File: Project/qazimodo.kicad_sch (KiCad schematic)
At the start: 24 parts, among them J1 AVR-ISP-6, J2 Conn_01x04_MountingPin, J3 USB_C_Receptacle_USB2.0, U1 ATmega32U4-M, Y1 Crystal_GND24_Small

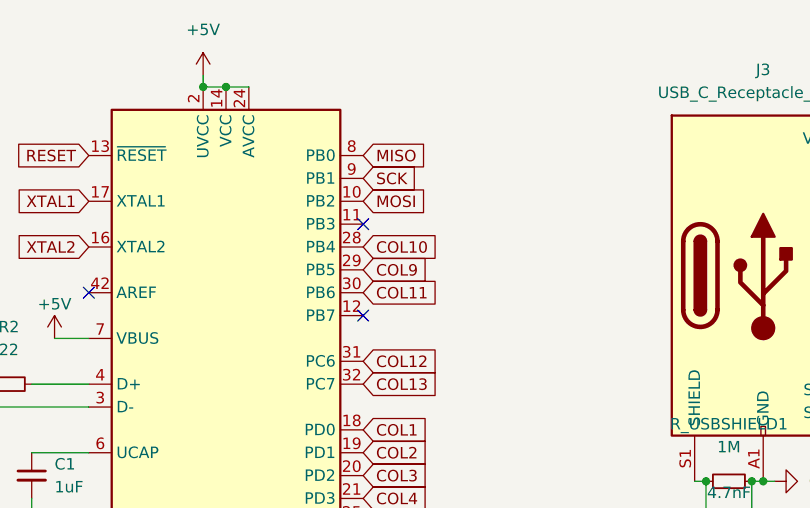
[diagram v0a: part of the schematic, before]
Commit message: matrix issues deteced and fixed, needs new silkscreen
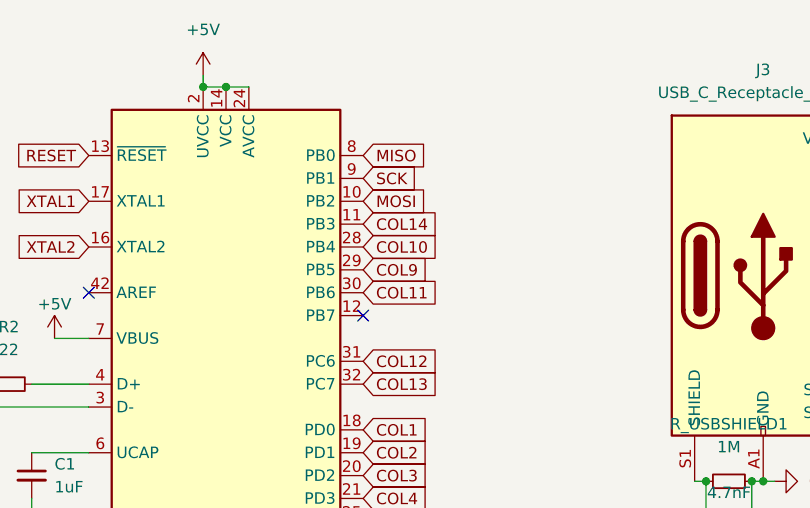
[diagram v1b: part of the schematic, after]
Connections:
- net COL14: now reaches U1.11 (PB3)
- no-connect marks 4 -> 3
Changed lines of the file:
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@@
   )
   (no_connect (at 39.37 45.085))
-  (no_connect (at 69.85 37.465))
   (no_connect (at 69.85 47.625))
   (no_connect (at 69.85 85.725))
@@
       (effects (font (size 1.27 1.27)) (justify left) hide)
     )
+  )
+  (global_label "COL14" (shape input) (at 69.85 37.465 0) (fields_autoplaced)
+    (effects (font (size 1.27 1.27)) (justify left))
+    (property "Intersheetrefs" "${INTERSHEET_REFS}" (at 78.8034 37.465 0)
+      (effects (font (size 1.27 1.27)) (justify left) hide)
+    )

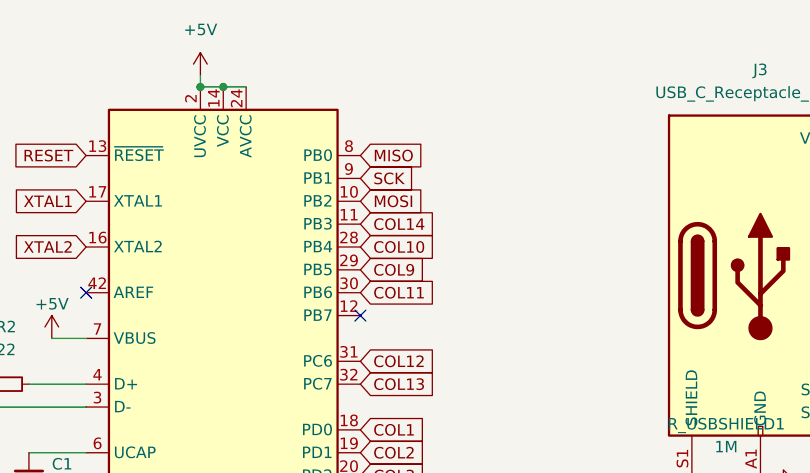
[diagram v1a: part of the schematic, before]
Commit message: reset pins corrected
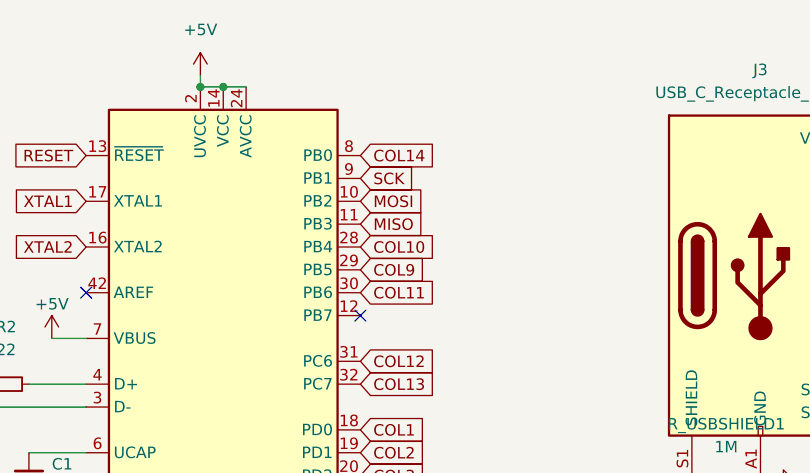
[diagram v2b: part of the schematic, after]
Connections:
- net COL14: now also U1.8 (PB0); no longer U1.11 (PB3)
- net MISO: now also U1.11 (PB3); no longer U1.8 (PB0)
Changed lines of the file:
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@@
     )
   )
-  (global_label "COL14" (shape input) (at 69.85 37.465 0) (fields_autoplaced)
+  (global_label "COL14" (shape input) (at 69.85 29.845 0) (fields_autoplaced)
     (effects (font (size 1.27 1.27)) (justify left))
-    (property "Intersheetrefs" "${INTERSHEET_REFS}" (at 78.8034 37.465 0)
+    (property "Intersheetrefs" "${INTERSHEET_REFS}" (at 78.8034 29.845 0)
       (effects (font (size 1.27 1.27)) (justify left) hide)
     )
@@
     )
   )
-  (global_label "MISO" (shape input) (at 69.85 29.845 0) (fields_autoplaced)
+  (global_label "MISO" (shape input) (at 69.85 37.465 0) (fields_autoplaced)
     (effects (font (size 1.27 1.27)) (justify left))
-    (property "Intersheetrefs" "${INTERSHEET_REFS}" (at 76.8593 29.7656 0)
+    (property "Intersheetrefs" "${INTERSHEET_REFS}" (at 76.8593 37.3856 0)
       (effects (font (size 1.27 1.27)) (justify left) hide)
     )

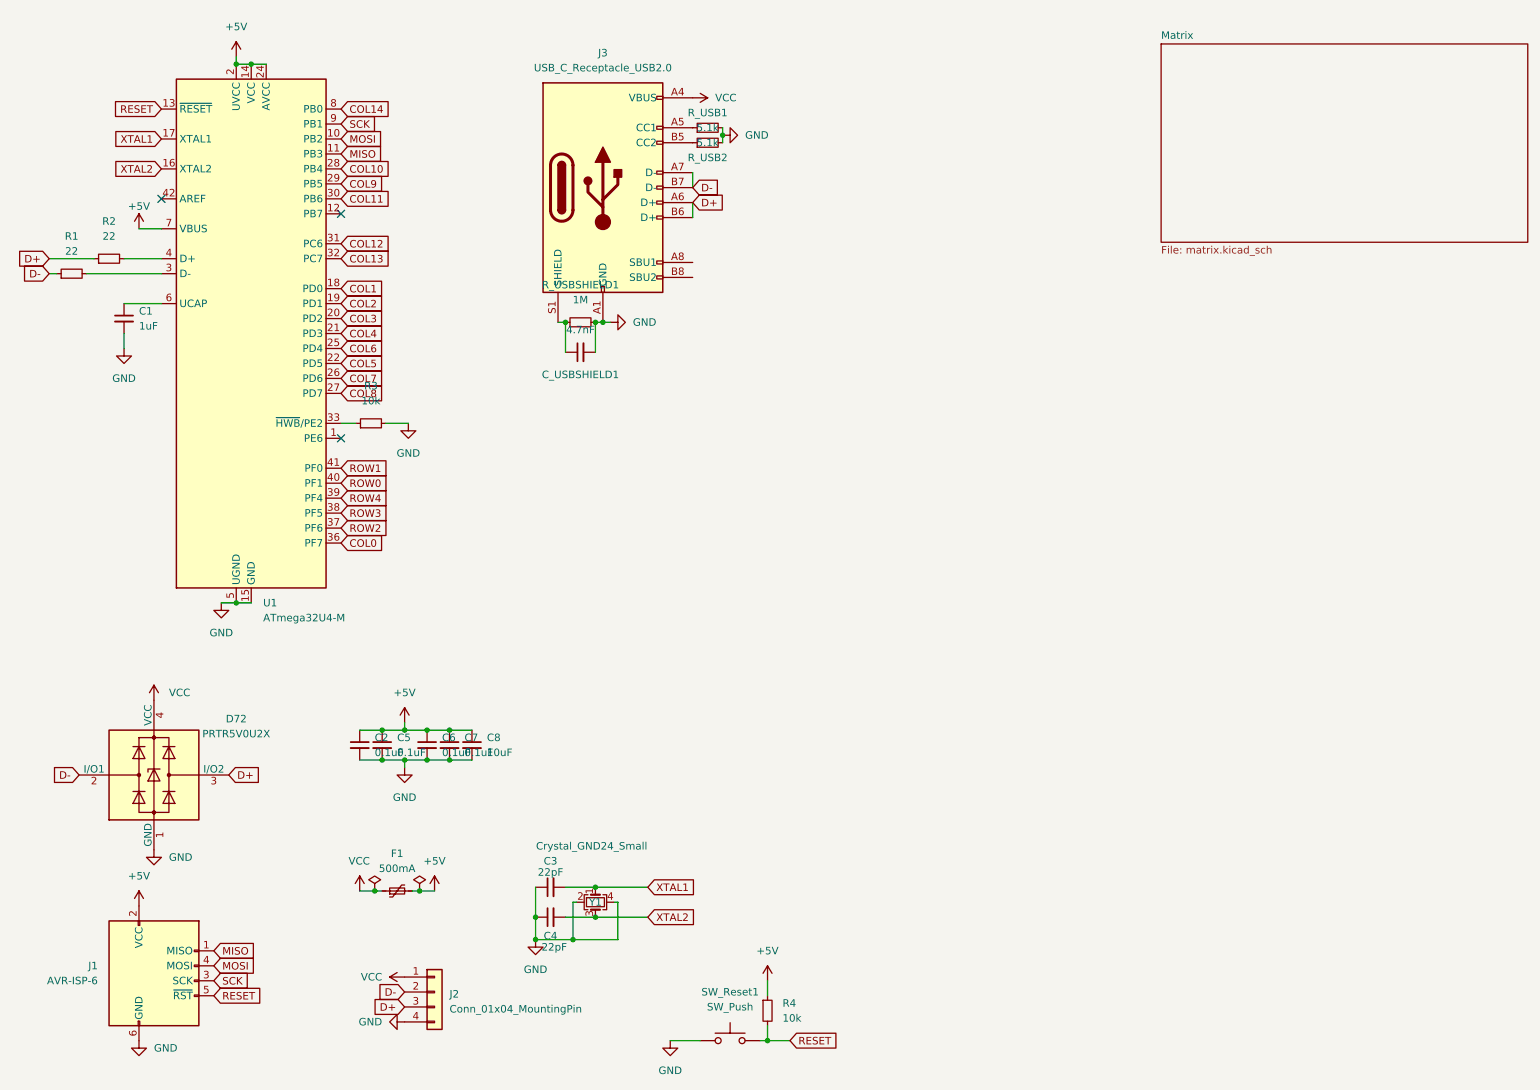
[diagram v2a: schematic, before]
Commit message: changed MCU to STM
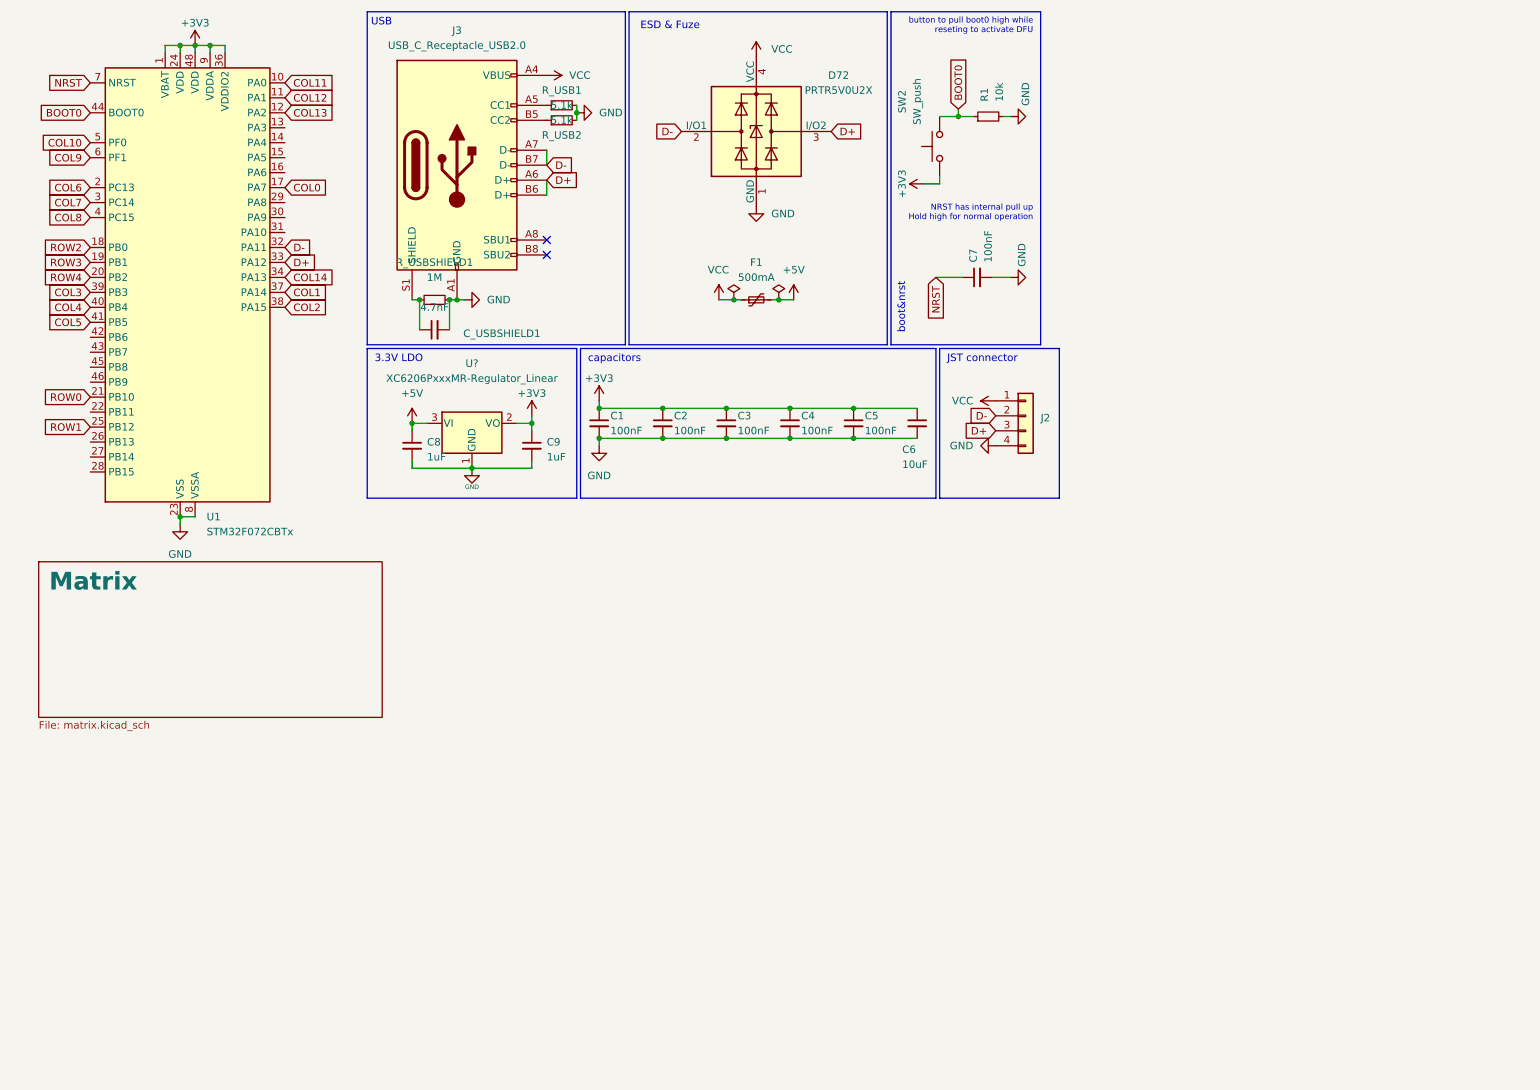
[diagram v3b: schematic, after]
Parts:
- removed C1: 1uF, Capacitor_SMD:C_0402_1005Metric, symbol ComboDiode:C_Small
- removed C2, C5, C6, C7: 0.1uF, Capacitor_SMD:C_0402_1005Metric, symbol ComboDiode:C_Small
- removed C3, C4: 22pF, Capacitor_SMD:C_0402_1005Metric, symbol ComboDiode:C_Small
- removed C8: 10uF, Capacitor_SMD:C_0402_1005Metric, symbol ComboDiode:C_Small
- removed J1: AVR-ISP-6, Keebio-Parts:ICSP_1.27mm, symbol Connector:AVR-ISP-6
- removed R1, R2: 22, Resistor_SMD:R_0402_1005Metric, symbol ComboDiode:R_Small
- removed R3, R4: 10k, Resistor_SMD:R_0402_1005Metric, symbol ComboDiode:R_Small
- removed SW_Reset1: SW_Push, random-keyboard-parts:SKQG-1155865, symbol Switch:SW_Push
- removed U1: ATmega32U4-M, Package_DFN_QFN:QFN-44-1EP_7x7mm_P0.5mm_EP5.2x5.2mm, symbol MCU_Microchip_ATmega:ATmega32U4-M
- removed Y1: Crystal_GND24_Small, Crystal:Crystal_SMD_3225-4Pin_3.2x2.5mm, symbol ComboDiode:Crystal_GND24_Small
- added C1, C2, C3, C4, C5, C7: 100nF, Capacitor_SMD:C_0402_1005Metric, symbol Device:C_Small
- added C6: 10uF, Capacitor_SMD:C_0402_1005Metric, symbol Device:C_Small
- added C8, C9: 1uF, Capacitor_SMD:C_0402_1005Metric, symbol Device:C_Small
- added R1: 10k, Resistor_SMD:R_0402_1005Metric, symbol Device:R_Small
- added SW2: SW_push, PCM_marbastlib-various:SW_SPST_SKQG_WithStem, symbol Switch:SW_Push
- added U1: STM32F072CBTx, Package_QFP:LQFP-48_7x7mm_P0.5mm, symbol MCU_ST_STM32F0:STM32F072CBTx
- added U?: XC6206PxxxMR-Regulator_Linear, Package_TO_SOT_SMD:SOT-23, symbol kicad-keyboard-parts:XC6206PxxxMR-Regulator_Linear
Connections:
- net +5V: now also C8.1, U?.3 (VI)
- net COL0: now also U1.17 (PA7)
- net COL1: now also U1.37 (PA14)
- net COL10: now also U1.5 (PF0)
- net COL11: now also U1.10 (PA0)
- net COL12: now also U1.11 (PA1)
- net COL13: now also U1.12 (PA2)
- net COL14: now also U1.34 (PA13)
- net COL2: now also U1.38 (PA15)
- net COL3: now also U1.39 (PB3)
- net COL4: now also U1.40 (PB4)
- net COL5: now also U1.41 (PB5)
- net COL6: now also U1.2 (PC13)
- net COL7: now also U1.3 (PC14)
- net COL8: now also U1.4 (PC15)
- net COL9: now also U1.6 (PF1)
- net D+: now also U1.33 (PA12)
- net D-: now also U1.32 (PA11)
- net GND: now also C1.2, C2.2, C3.2, C4.2, C5.2, C6.2, C7.2, C8.2, C9.2, R1.2, U1.23 (VSS), U1.35 (VSS), U1.47 (VSS), U1.8 (VSSA), U?.1 (GND)
- net ROW0: now also U1.21 (PB10)
- net ROW1: now also U1.25 (PB12)
- net ROW2: now also U1.18 (PB0)
- net ROW3: now also U1.19 (PB1)
- net ROW4: now also U1.20 (PB2)
- new net +3V3: C1.1, C2.1, C3.1, C4.1, C5.1, C6.1, C9.1, SW2.1, U1.1 (VBAT), U1.24 (VDD), U1.36 (VDDIO2), U1.48 (VDD), U1.9 (VDDA), U?.2 (VO)
- new net BOOT0: R1.1, SW2.2, U1.44 (BOOT0)
- new net NRST: C7.1, U1.7 (NRST)
- no-connect marks 3 -> 2
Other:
- note added: "3.3V LDO"
- note added: "ESD & Fuze"
- note added: "JST connector"
- note added: "NRST has internal pull up Hold high for normal operation"
- note added: "USB"
- note added: "boot&nrst"
- note added: "button to pull boot0 high while reseting to activate DFU"
- note added: "capacitors"
- moved on the sheet: C_USBSHIELD1, D72, F1, J2, J3, R_USB1, R_USB2, R_USBSHIELD1

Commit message: revision wip
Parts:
- removed C_USBSHIELD1: 4.7nF, Capacitor_SMD:C_0402_1005Metric, symbol Device:C_Small
- removed R_USBSHIELD1: 1M, Resistor_SMD:R_0402_1005Metric, symbol Device:R_Small
- C1, C2, C3, C4, C5, C6, C7, C8, C9: footprint Capacitor_SMD:C_0402_1005Metric -> Capacitor_SMD:C_0805_2012Metric_Pad1.18x1.45mm_HandSolder
- D72: footprint Package_TO_SOT_SMD:SOT-143 -> Package_TO_SOT_SMD:SOT-143_Handsoldering
- F1: footprint Fuse:Fuse_1206_3216Metric -> Fuse:Fuse_1206_3216Metric_Pad1.42x1.75mm_HandSolder
- R1, R_USB1, R_USB2: footprint Resistor_SMD:R_0402_1005Metric -> Resistor_SMD:R_0805_2012Metric_Pad1.20x1.40mm_HandSolder
- U?: footprint Package_TO_SOT_SMD:SOT-23 -> Package_TO_SOT_SMD:SOT-23_Handsoldering
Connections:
- net GND: now also J3.S1 (SHIELD)

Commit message: revision work
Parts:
- added SW2: SW_push, Connector_PinHeader_2.54mm:PinHeader_1x02_P2.54mm_Vertical, symbol Switch:SW_Push
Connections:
- net +3V3: now also SW2.1
- net BOOT0: now also SW2.2
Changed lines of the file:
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@@
   (junction (at 146.05 85.725) (diameter 0) (color 0 0 0 0)
+  )
+  (junction (at 172.7168 31.115) (diameter 0) (color 0 0 0 0)
+  )
+  (junction (at 171.45 41.275) (diameter 0) (color 0 0 0 0)
   )
   (junction (at 124.46 85.725) (diameter 0) (color 0 0 0 0)
@@
     (stroke (width 0) (type default))
   )
+  (wire (pts (xy 171.45 41.275) (xy 172.7168 41.275))
+    (stroke (width 0) (type default))
+  )
   (wire (pts (xy 50.165 19.05) (xy 50.165 20.32))
     (stroke (width 0) (type default))
@@
     (stroke (width 0) (type default))
   )
+  (wire (pts (xy 172.7168 31.115) (xy 174.625 31.115))
+    (stroke (width 0) (type default))
+  )
   (wire (pts (xy 99.695 83.185) (xy 102.235 83.185))
     (stroke (width 0) (type solid))
@@
     (stroke (width 0) (type default))
   )
-  (wire (pts (xy 171.45 31.115) (xy 174.625 31.115))
+  (wire (pts (xy 171.45 31.115) (xy 172.7168 31.115))
     (stroke (width 0) (type default))
   )
@@
     )
   )
+  (symbol (lib_id "Switch:SW_Push") (at 172.7168 36.195 90) (unit 1)
+    (in_bom yes) (on_board yes) (dnp no)
+    (property "Reference" "SW2" (at 166.3668 28.575 0)
+      (effects (font (size 1.27 1.27)))
+    )
+    (property "Value" "SW_push" (at 168.9068 28.575 0)
+      (effects (font (size 1.27 1.27)))
+    )
+    (property "Footprint" "Connector_PinHeader_2.54mm:PinHeader_1x02_P2.54mm_Vertical" (at 167.6368 36.195 0)
+      (effects (font (size 1.27 1.27)) hide)
+    )
+    (property "Datasheet" "~" (at 167.6368 36.195 0)
+      (effects (font (size 1.27 1.27)) hide)
+    )
+    (pin "1")
+    (pin "2")
+    (instances
+      (project "flexi project"
+        (path "/a497b2b5-f448-43a1-9535-e77ad9f58f07"
+          (reference "SW2") (unit 1)
+        )
+      )
+      (project "qazimodo"
+        (path "/edc62a67-076c-4011-9c94-45c426528f86"
+          (reference "SW2") (unit 1)
+        )
+      )
+    )
+  )

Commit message: update
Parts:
- J3: footprint Connector_USB:USB_C_Receptacle_HRO_TYPE-C-31-M-12 -> Connector_USB:USB_C_Receptacle_GCT_USB4085
